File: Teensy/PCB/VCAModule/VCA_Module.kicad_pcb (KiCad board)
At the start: 2 copper layers, 45.7 x 106.7 mm, 51 parts, among them J1 Power_Connector_2x3, U1 Teensy4.0

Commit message: Generated Gerbers
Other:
- board text added: "+"

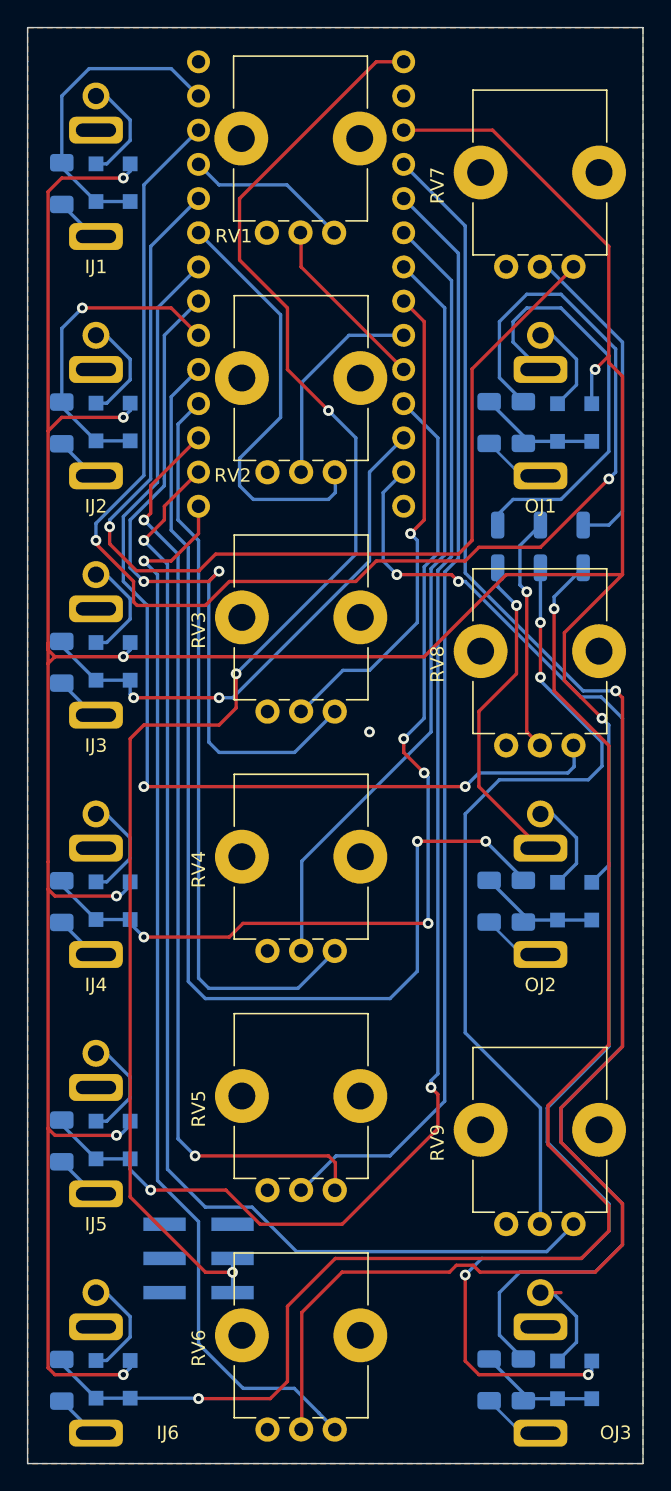
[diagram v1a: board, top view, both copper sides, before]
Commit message: Made NPTH holes 0.5mm bigger; adjusted diode pads for better solderability
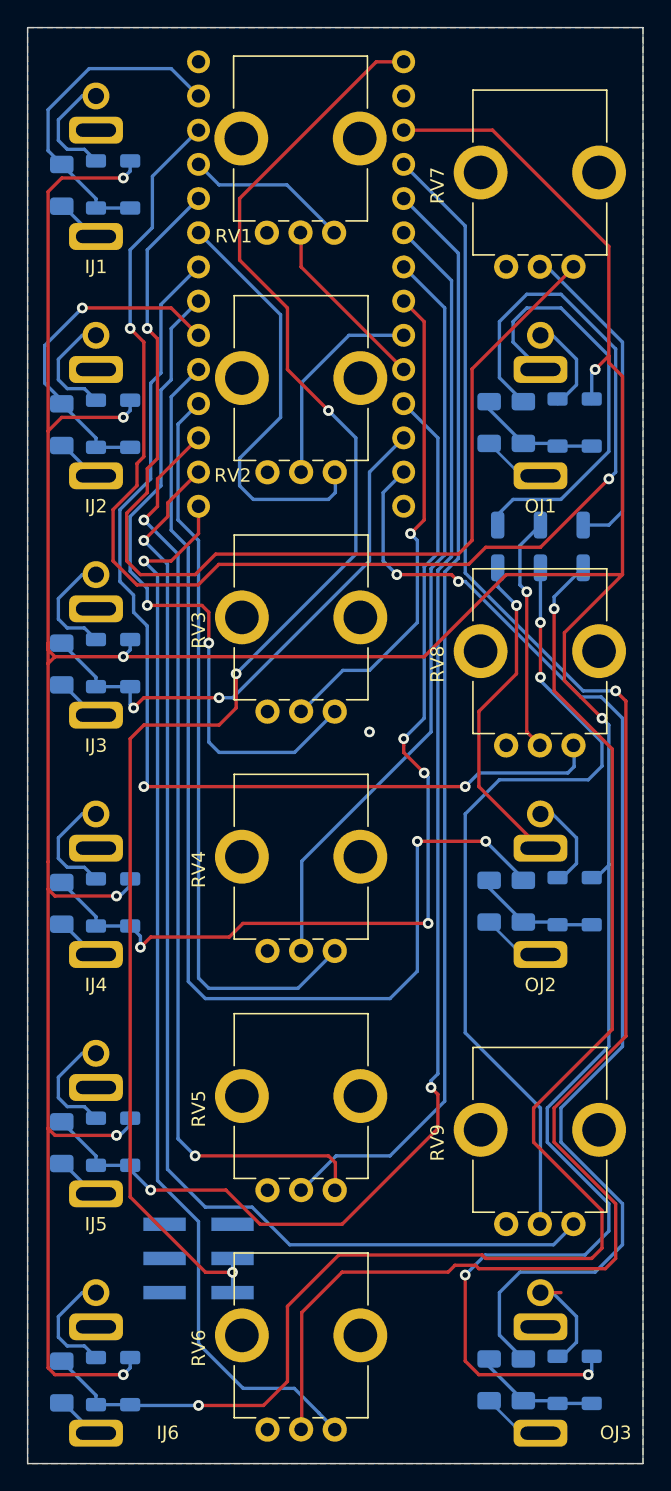
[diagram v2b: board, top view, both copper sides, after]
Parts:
- ID1, ID10, ID11, ID12, ID2, ID3, ID4, ID5, ID6, ID7, ID8, ID9, OD1, OD2, OD3, OD4, OD5, OD6: footprint Diode_SMD:D_SOD-123F -> Misc:D_SOD-123 Handsolder
- moved ID10 0.13 mm to (43.2, 141.2)
- moved ID11 0.13 mm to (40.6, 159.0)
- moved ID12 0.13 mm to (43.2, 159.0)
- moved ID9 0.13 mm to (40.6, 141.2)
- moved ID1 0.13 mm to (40.6, 70.1)
- moved ID2 0.13 mm to (43.2, 70.1)
- moved ID3 0.13 mm to (40.6, 87.9)
- moved ID4 0.13 mm to (43.2, 87.9)
- moved ID5 0.13 mm to (40.6, 105.6)
- moved ID6 0.13 mm to (43.2, 105.6)
- moved ID7 0.13 mm to (40.6, 123.4)
- moved ID8 0.13 mm to (43.2, 123.4)
- moved IR1 0.13 mm to (38.1, 70.1)
- moved IR2 0.13 mm to (38.1, 87.9)
- moved IR3 0.13 mm to (38.1, 105.7)
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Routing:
- net /T6: track 53.2 -> 50.6 mm
- net GND: track 71.8 -> 74.3 mm
- net /T1: track 106.4 -> 104.0 mm
- net /T25: track 106.1 -> 108.0 mm
- net /T7: track 23.6 -> 25.1 mm
- net /T0: track 23.3 -> 24.6 mm
- net /T16: track 71.2 -> 72.3 mm
- net /T15: track 39.8 -> 40.8 mm
